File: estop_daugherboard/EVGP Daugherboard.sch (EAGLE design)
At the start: 30 parts, among them J2 AVR_SPI_PROG_3X2PTH, J3 UX60-MB-5S8, U1 ATMEGA32U4-AU, X1 TSX-3225 16.0000MF18X-AC0

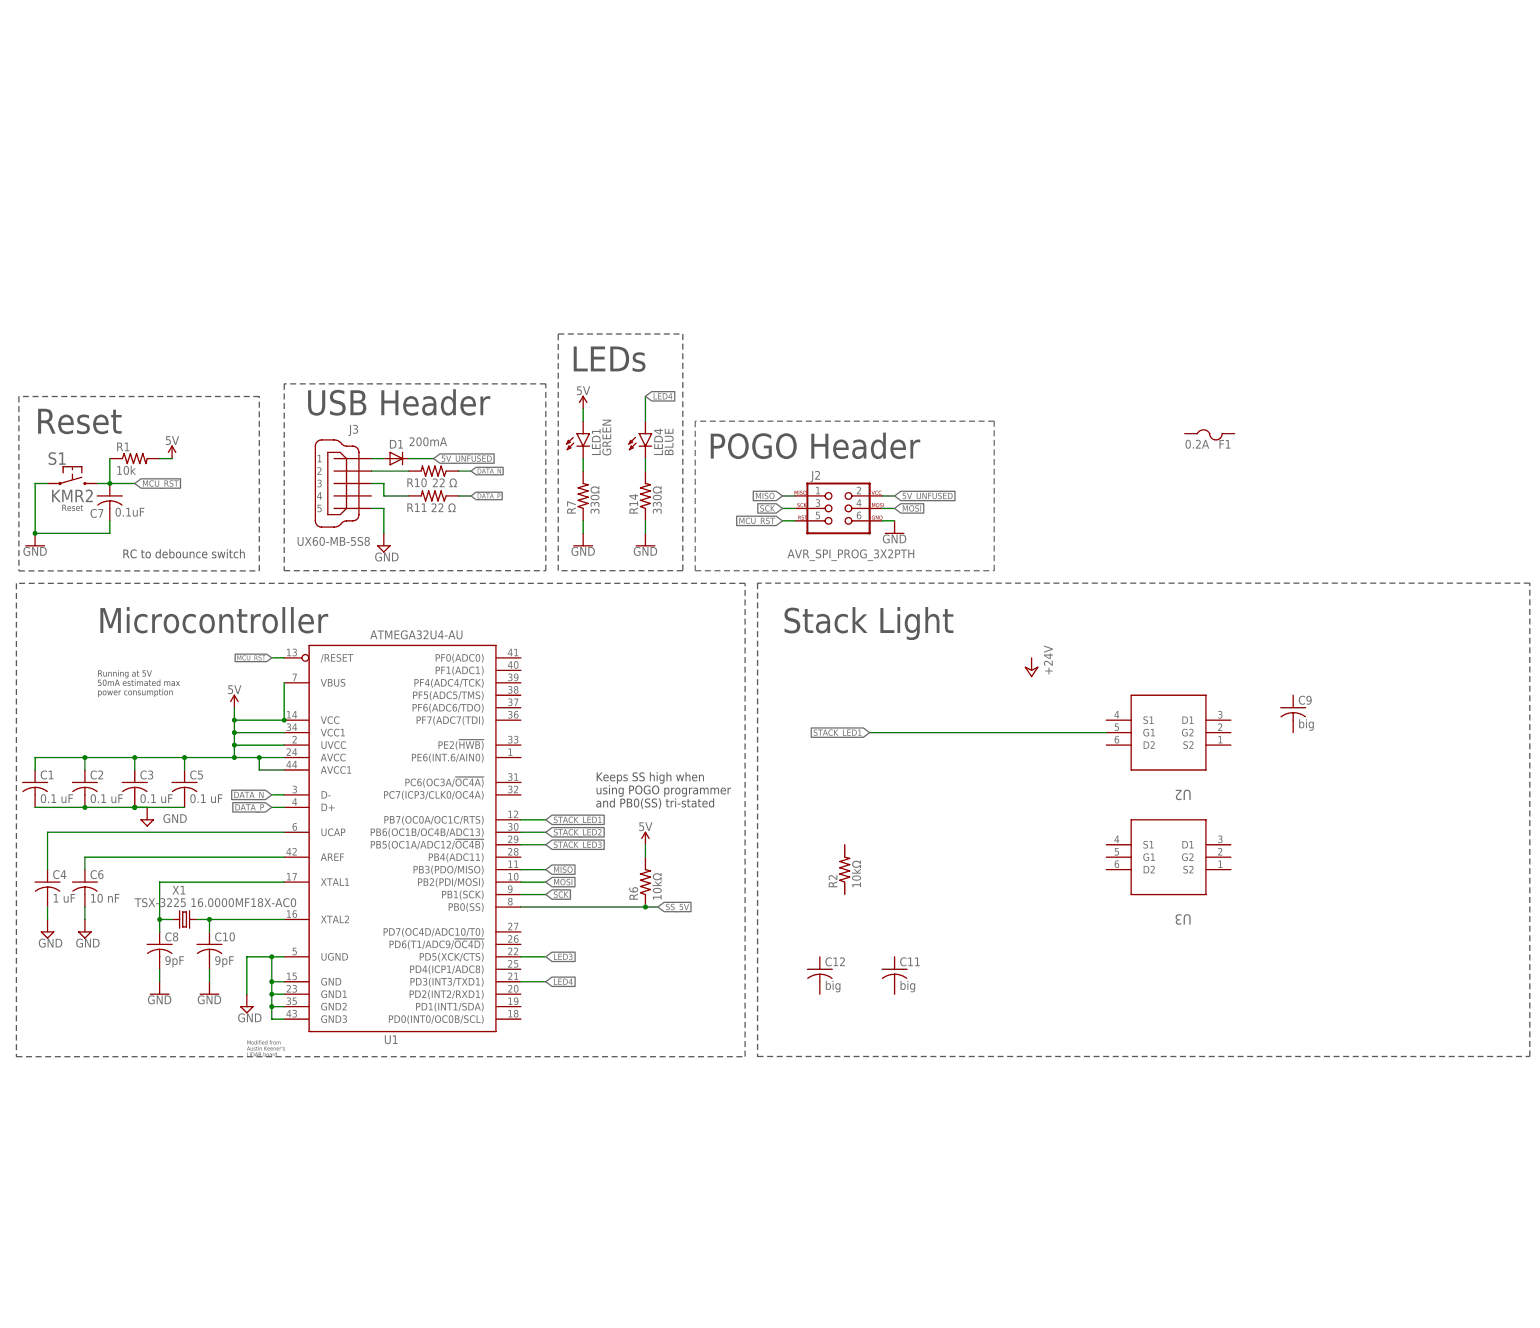
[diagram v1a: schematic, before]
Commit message: schematic updates, header and and gates
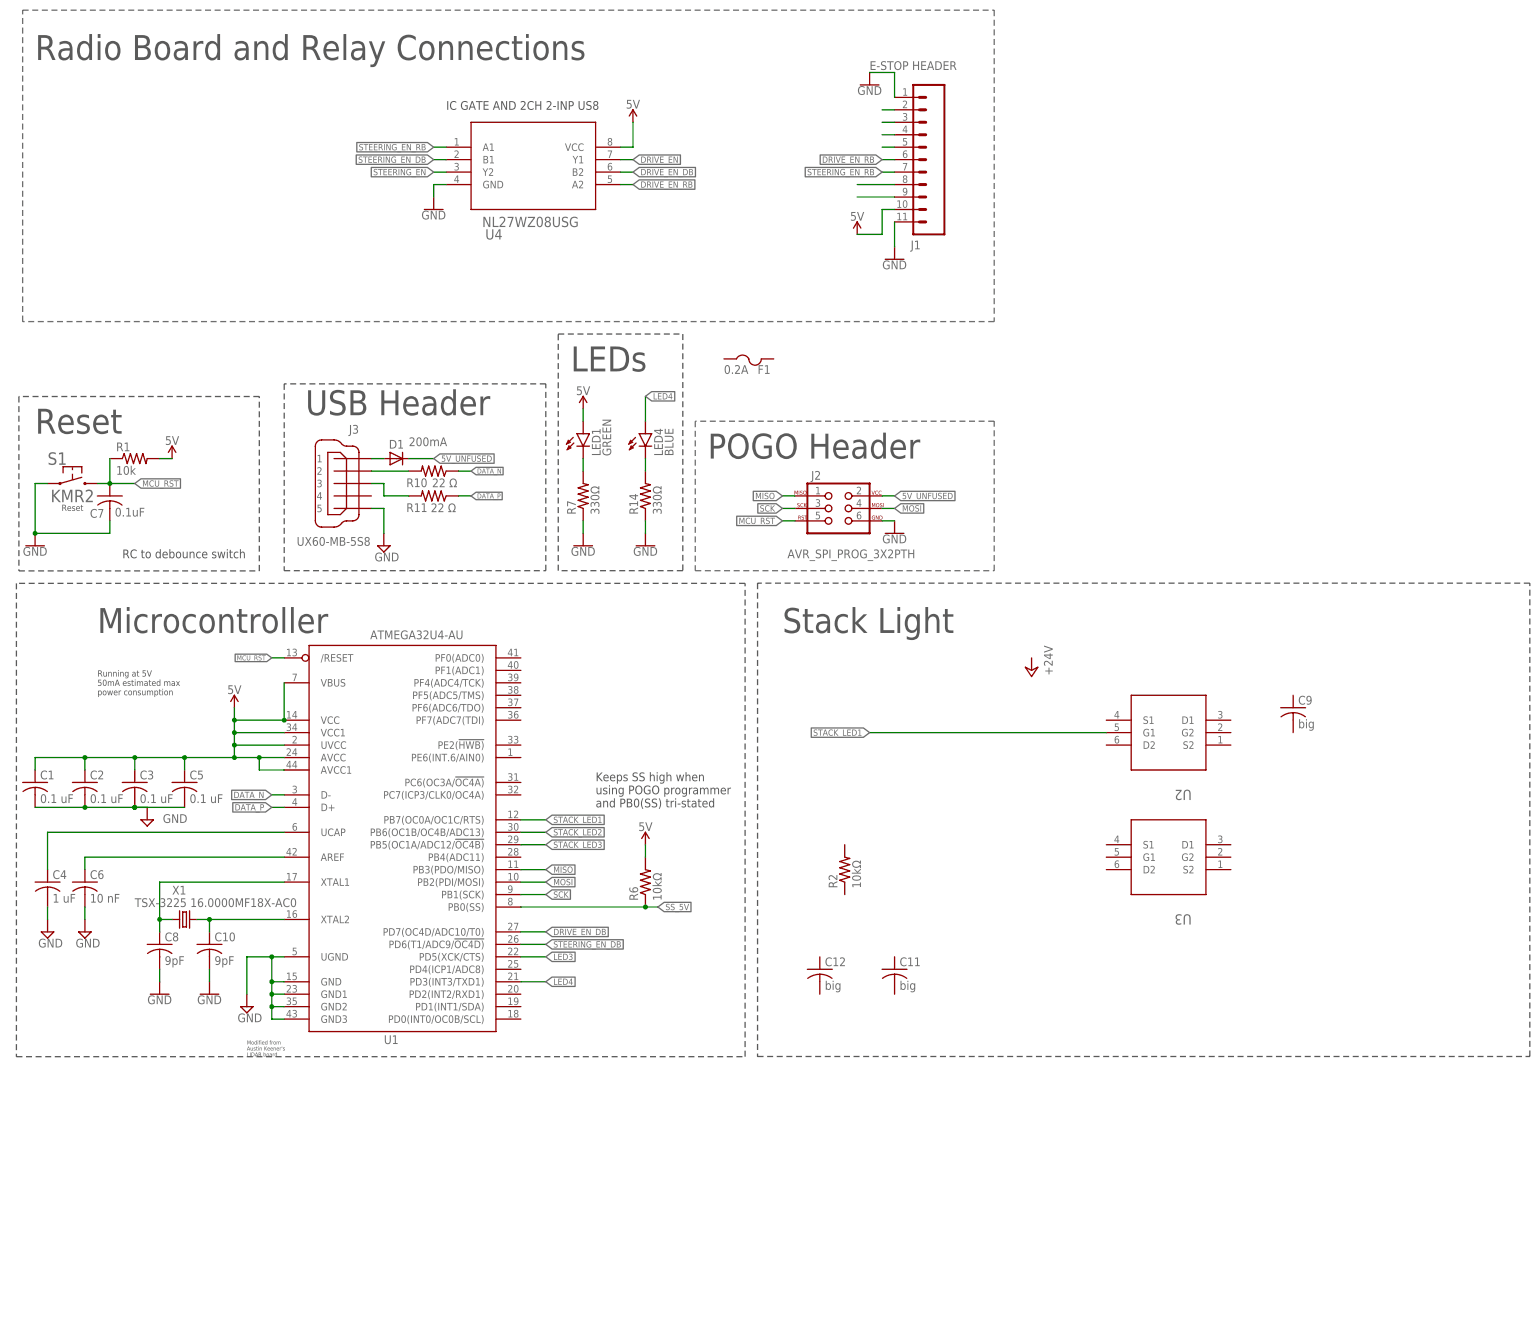
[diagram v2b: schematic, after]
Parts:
- added J1: E-STOP HEADER, SparkFun-Connectors:CONN_11
- added U4: NL27WZ08USG, DownloadedFiles:NL27WZ08USG
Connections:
- new net DIO_1: J1.3
- new net DIO_2: J1.4
- new net DIO_3: J1.5
- new net DIO_6_R: J1.8
- new net DIO_7_R: J1.9
- new net DRIVE_EN: U4.Y1
- new net DRIVE_EN_DB: U1.PD7(OC4D/ADC10/T0), U4.B2
- new net DRIVE_EN_RB: J1.6, U4.A2
- new net MCU_RST1: J1.2
- new net STEERING_EN: U4.Y2
- new net STEERING_EN_DB: U1.PD6(T1/ADC9/!OC4D), U4.B1
- new net STEERING_EN_RB: J1.7, U4.A1
- net 5V: now also J1.10, U4.VCC
- net GND: now also J1.1, J1.11, U4.GND
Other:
- note added: "IC GATE AND 2CH 2-INP US8"
- note added: "Radio Board and Relay Connections"
- moved on the sheet: F1
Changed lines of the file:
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@@
 <?xml version="1.0" encoding="utf-8"?>
 <!DOCTYPE eagle SYSTEM "eagle.dtd">
-<eagle version="9.5.1">
+<eagle version="9.5.0">
 <drawing>
 <settings>
@@
 <part name="P+1" library="supply1" library_urn="urn:adsk.eagle:library:371" deviceset="+24V" device=""/>
 <part name="F1" library="adafruit" library_urn="urn:adsk.eagle:library:420" deviceset="PTCFUSE" device="-1206" package3d_urn="urn:adsk.eagle:package:6240569/1" value="0.2A"/>
+<part name="GND4" library="SparkFun-PowerSymbols" deviceset="GND" device=""/>
+<part name="J1" library="SparkFun-Connectors" library_urn="urn:adsk.eagle:library:513" deviceset="CONN_11" device="" package3d_urn="urn:adsk.eagle:package:38251/1" value="E-STOP HEADER"/>
+<part name="GND2" library="SparkFun-PowerSymbols" deviceset="GND" device=""/>
+<part name="SUPPLY8" library="SparkFun-PowerSymbols" deviceset="5V" device=""/>
+<part name="U4" library="DownloadedFiles" deviceset="NL27WZ08USG" device=""/>
+<part name="SUPPLY9" library="SparkFun-PowerSymbols" deviceset="5V" device=""/>
+<part name="GND3" library="SparkFun-PowerSymbols" deviceset="GND" device=""/>
 </parts>
 <sheets>
@@
 <wire x1="322.58" y1="10.16" x2="322.58" y2="106.68" width="0.1524" layer="97" style="shortdash"/>
 <wire x1="322.58" y1="106.68" x2="165.1" y2="106.68" width="0.1524" layer="97" style="shortdash"/>
+<wire x1="15.24" y1="160.02" x2="15.24" y2="223.52" width="0.1524" layer="95" style="shortdash"/>
+<wire x1="15.24" y1="223.52" x2="213.36" y2="223.52" width="0.1524" layer="95" style="shortdash"/>
+<wire x1="213.36" y1="223.52" x2="213.36" y2="160.02" width="0.1524" layer="95" style="shortdash"/>
+<wire x1="213.36" y1="160.02" x2="15.24" y2="160.02" width="0.1524" layer="95" style="shortdash"/>
+<text x="17.78" y="213.36" size="5.08" layer="97">Radio Board and Relay Connections</text>
+<text x="101.6" y="203.2" size="1.778" layer="97">IC GATE AND 2CH 2-INP US8</text>
 </plain>
 <instances>
@@
 <attribute name="VALUE" x="223.52" y="93.98" size="1.778" layer="96" rot="R270"/>
 </instance>
-<instance part="F1" gate="G$1" x="257.302" y="134.62" smashed="yes">
-<attribute name="VALUE" x="252.222" y="134.112" size="1.778" layer="96"/>
-<attribute name="NAME" x="259.08" y="134.112" size="1.778" layer="95"/>
+<instance part="F1" gate="G$1" x="163.322" y="149.86" smashed="yes">
+<attribute name="VALUE" x="158.242" y="149.352" size="1.778" layer="96"/>
+<attribute name="NAME" x="165.1" y="149.352" size="1.778" layer="95"/>
+</instance>
+<instance part="GND4" gate="1" x="193.04" y="172.72" smashed="yes">
+<attribute name="VALUE" x="193.04" y="172.466" size="1.778" layer="96" align="top-center"/>
+</instance>
+<instance part="J1" gate="G$1" x="203.2" y="193.04" smashed="yes" rot="R180">
+<attribute name="VALUE" x="205.74" y="213.106" size="1.778" layer="96" font="vector" rot="R180"/>
+<attribute name="NAME" x="198.374" y="176.53" size="1.778" layer="95" font="vector" rot="R180"/>
+</instance>
+<instance part="GND2" gate="1" x="187.96" y="208.28" smashed="yes">
+<attribute name="VALUE" x="187.96" y="208.026" size="1.778" layer="96" align="top-center"/>
+</instance>
+<instance part="SUPPLY8" gate="G$1" x="185.42" y="177.8" smashed="yes">
+<attribute name="VALUE" x="185.42" y="180.594" size="1.778" layer="96" align="bottom-center"/>
+</instance>
+<instance part="U4" gate="A" x="99.06" y="195.58" smashed="yes">
+<attribute name="NAME" x="109.5756" y="176.7586" size="2.0828" layer="95" ratio="6" rot="SR0"/>
+<attribute name="VALUE" x="108.9406" y="179.2986" size="2.0828" layer="96" ratio="6" rot="SR0"/>
+</instance>
+<instance part="SUPPLY9" gate="G$1" x="139.7" y="200.66" smashed="yes">
+<attribute name="VALUE" x="139.7" y="203.454" size="1.778" layer="96" align="bottom-center"/>
+</instance>
+<instance part="GND3" gate="1" x="99.06" y="182.88" smashed="yes">
+<attribute name="VALUE" x="99.06" y="182.626" size="1.778" layer="96" align="top-center"/>
 </instance>
 </instances>
@@
 <pinref part="GND10" gate="1" pin="GND"/>
 <wire x1="142.24" y1="119.38" x2="142.24" y2="116.84" width="0.1524" layer="91"/>
+</segment>
+<segment>
+<wire x1="187.96" y1="210.82" x2="193.04" y2="210.82" width="0.1524" layer="91"/>
+<pinref part="J1" gate="G$1" pin="1"/>
+<wire x1="193.04" y1="210.82" x2="193.04" y2="205.74" width="0.1524" layer="91"/>
+<pinref part="GND2" gate="1" pin="GND"/>
+</segment>
+<segment>
+<pinref part="GND4" gate="1" pin="GND"/>
+<pinref part="J1" gate="G$1" pin="11"/>
+<wire x1="193.04" y1="175.26" x2="193.04" y2="180.34" width="0.1524" layer="91"/>
+</segment>
+<segment>
+<pinref part="GND3" gate="1" pin="GND"/>
+<pinref part="U4" gate="A" pin="GND"/>
+<wire x1="99.06" y1="185.42" x2="99.06" y2="187.96" width="0.1524" layer="91"/>
+<wire x1="99.06" y1="187.96" x2="101.6" y2="187.96" width="0.1524" layer="91"/>
 </segment>
 </net>
@@
 <pinref part="R6" gate="G$1" pin="2"/>
 </segment>
+<segment>
+<pinref part="SUPPLY8" gate="G$1" pin="5V"/>
+<wire x1="185.42" y1="177.8" x2="190.5" y2="177.8" width="0.1524" layer="91"/>
+<pinref part="J1" gate="G$1" pin="10"/>
+<wire x1="193.04" y1="182.88" x2="190.5" y2="182.88" width="0.1524" layer="91"/>
+<wire x1="190.5" y1="177.8" x2="190.5" y2="182.88" width="0.1524" layer="91"/>
+</segment>
+<segment>
+<pinref part="U4" gate="A" pin="VCC"/>
+<wire x1="137.16" y1="195.58" x2="139.7" y2="195.58" width="0.1524" layer="91"/>
+<wire x1="139.7" y1="195.58" x2="139.7" y2="200.66" width="0.1524" layer="91"/>
+<pinref part="SUPPLY9" gate="G$1" pin="5V"/>
+</segment>
 </net>
 <net name="MCU_RST" class="0">
@@
 </segment>
 </net>
+<net name="MCU_RST1" class="0">
+<segment>
+<wire x1="193.04" y1="203.2" x2="190.5" y2="203.2" width="0.1524" layer="91"/>
+<pinref part="J1" gate="G$1" pin="2"/>
+</segment>
+</net>
+<net name="DIO_3" class="0">
+<segment>
+<wire x1="190.5" y1="195.58" x2="193.04" y2="195.58" width="0.1524" layer="91"/>
+<pinref part="J1" gate="G$1" pin="5"/>
+</segment>
+</net>
+<net name="DIO_2" class="0">
+<segment>
+<wire x1="190.5" y1="198.12" x2="193.04" y2="198.12" width="0.1524" layer="91"/>
+<pinref part="J1" gate="G$1" pin="4"/>
+</segment>
+</net>
+<net name="DIO_1" class="0">
+<segment>
+<wire x1="190.5" y1="200.66" x2="193.04" y2="200.66" width="0.1524" layer="91"/>
+<pinref part="J1" gate="G$1" pin="3"/>
+</segment>
+</net>
+<net name="DIO_6_R" class="0">
+<segment>
+<wire x1="185.42" y1="187.96" x2="193.04" y2="187.96" width="0.1524" layer="91"/>
+<pinref part="J1" gate="G$1" pin="8"/>
+</segment>
+</net>
+<net name="DIO_7_R" class="0">
+<segment>
+<wire x1="185.42" y1="185.42" x2="193.04" y2="185.42" width="0.1524" layer="91"/>
+<pinref part="J1" gate="G$1" pin="9"/>
+</segment>
+</net>
+<net name="DRIVE_EN_RB" class="0">
+<segment>
+<wire x1="190.5" y1="193.04" x2="193.04" y2="193.04" width="0.1524" layer="91"/>
+<pinref part="J1" gate="G$1" pin="6"/>
+<label x="190.5" y="193.04" size="1.27" layer="95" rot="R180" xref="yes"/>
+</segment>
+<segment>
+<pinref part="U4" gate="A" pin="A2"/>
+<wire x1="137.16" y1="187.96" x2="139.7" y2="187.96" width="0.1524" layer="91"/>
+<label x="139.7" y="187.96" size="1.27" layer="95" xref="yes"/>
+</segment>
+</net>
+<net name="STEERING_EN_RB" class="0">
+<segment>
+<wire x1="190.5" y1="190.5" x2="193.04" y2="190.5" width="0.1524" layer="91"/>
+<pinref part="J1" gate="G$1" pin="7"/>
+<label x="190.5" y="190.5" size="1.27" layer="95" rot="R180" xref="yes"/>
+</segment>
+<segment>
+<pinref part="U4" gate="A" pin="A1"/>
+<wire x1="101.6" y1="195.58" x2="99.06" y2="195.58" width="0.1524" layer="91"/>
+<label x="99.06" y="195.58" size="1.27" layer="95" rot="R180" xref="yes"/>
+</segment>
+</net>
+<net name="DRIVE_EN_DB" class="0">
+<segment>
+<pinref part="U1" gate="G$1" pin="PD7(OC4D/ADC10/T0)"/>
+<wire x1="116.84" y1="35.56" x2="121.92" y2="35.56" width="0.1524" layer="91"/>
+<label x="121.92" y="35.56" size="1.27" layer="95" xref="yes"/>
+</segment>
+<segment>
+<pinref part="U4" gate="A" pin="B2"/>
+<wire x1="137.16" y1="190.5" x2="139.7" y2="190.5" width="0.1524" layer="91"/>
+<label x="139.7" y="190.5" size="1.27" layer="95" xref="yes"/>
+</segment>
+</net>
+<net name="STEERING_EN_DB" class="0">
+<segment>
+<pinref part="U1" gate="G$1" pin="PD6(T1/ADC9/!OC4D)"/>
+<wire x1="116.84" y1="33.02" x2="121.92" y2="33.02" width="0.1524" layer="91"/>
+<label x="121.92" y="33.02" size="1.27" layer="95" xref="yes"/>
+</segment>
+<segment>
+<pinref part="U4" gate="A" pin="B1"/>
+<wire x1="101.6" y1="193.04" x2="99.06" y2="193.04" width="0.1524" layer="91"/>
+<label x="99.06" y="193.04" size="1.27" layer="95" rot="R180" xref="yes"/>
+</segment>
+</net>
+<net name="STEERING_EN" class="0">
+<segment>
+<pinref part="U4" gate="A" pin="Y2"/>
+<wire x1="101.6" y1="190.5" x2="99.06" y2="190.5" width="0.1524" layer="91"/>
+<label x="99.06" y="190.5" size="1.27" layer="95" rot="R180" xref="yes"/>
+</segment>
+</net>
+<net name="DRIVE_EN" class="0">
+<segment>
+<pinref part="U4" gate="A" pin="Y1"/>
+<wire x1="137.16" y1="193.04" x2="139.7" y2="193.04" width="0.1524" layer="91"/>
+<label x="139.7" y="193.04" size="1.27" layer="95" xref="yes"/>
+</segment>
+</net>
